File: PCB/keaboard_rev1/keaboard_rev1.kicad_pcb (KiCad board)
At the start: 2 copper layers, 6 parts, among them U1 Arduino Pro Micro

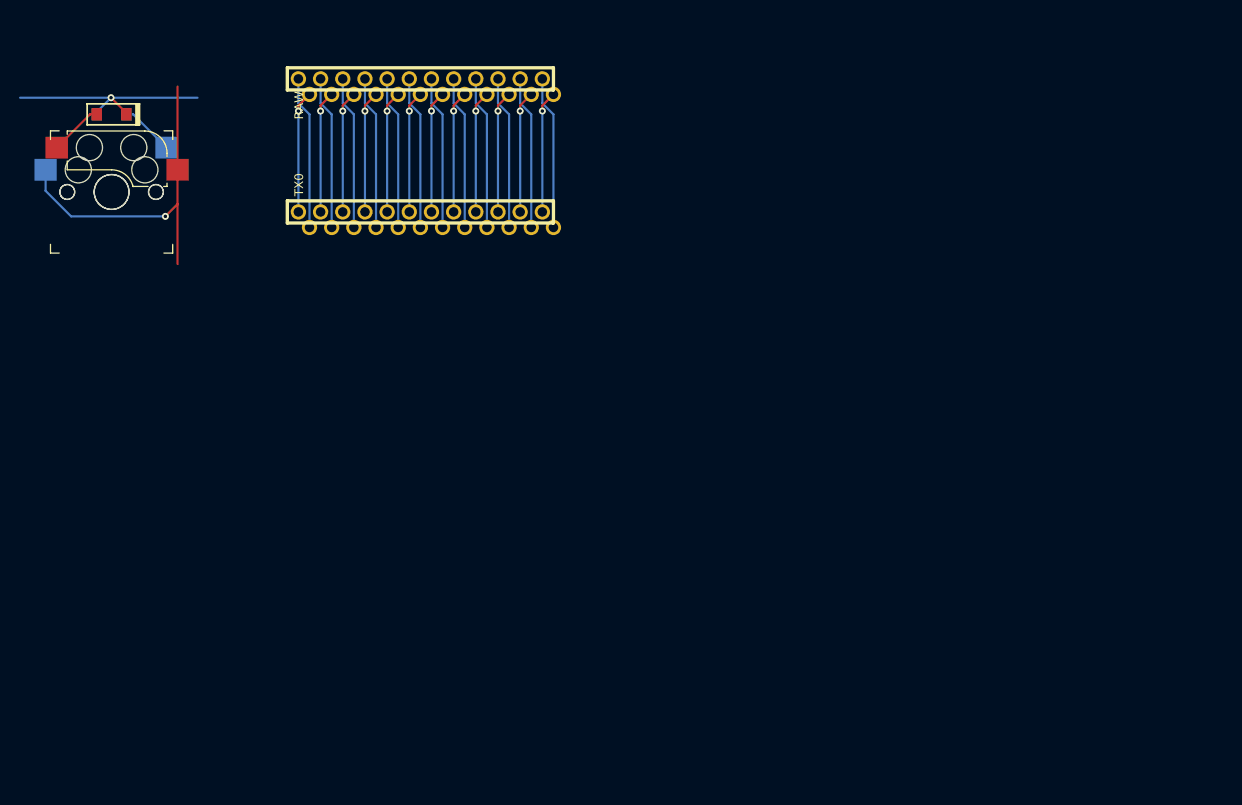
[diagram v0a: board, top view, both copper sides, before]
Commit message: Keyboard layout and cutout
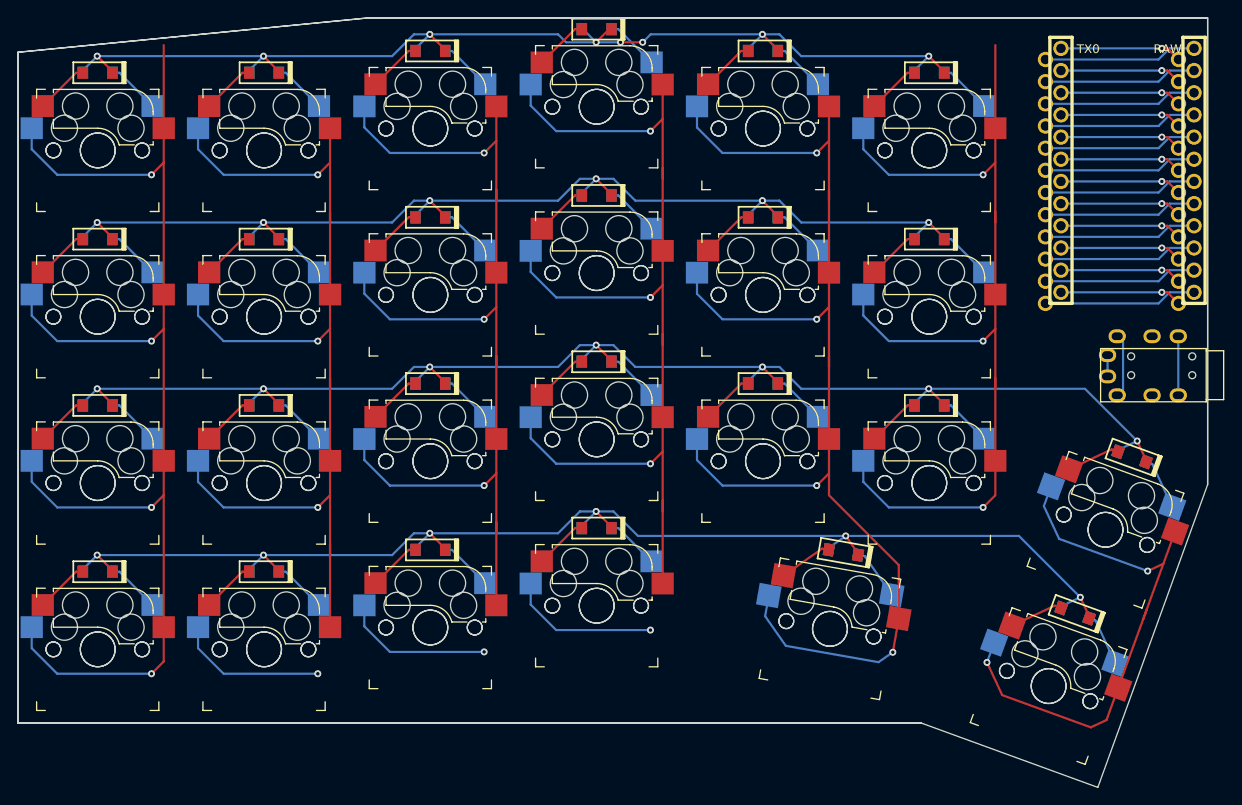
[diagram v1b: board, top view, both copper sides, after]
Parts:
- removed the D_SOD123 at (39.7, 38.7) (x2)
- removed the REF** at (39.7, 47.6) (x2)
- added D_SOD123: VAL**, keyboard_parts:D_SOD123, B.Cu at (150.1, 95.9)
- added D_SOD123: VAL**, keyboard_parts:D_SOD123, F.Cu at (133.3, 53.0)
- added D_SOD123: VAL**, keyboard_parts:D_SOD123, F.Cu at (114.3, 50.5)
- added D_SOD123: VAL**, keyboard_parts:D_SOD123, F.Cu at (95.2, 48.0)
- added D_SOD123: VAL**, keyboard_parts:D_SOD123, F.Cu at (133.3, 34.0)
- added D_SOD123: VAL**, keyboard_parts:D_SOD123, F.Cu at (114.3, 31.5)
- added D_SOD123: VAL**, keyboard_parts:D_SOD123, B.Cu at (123.5, 88.9)
- added D_SOD123: VAL**, keyboard_parts:D_SOD123, B.Cu at (95.2, 86.1)
- added D_SOD123: VAL**, keyboard_parts:D_SOD123, B.Cu at (133.3, 72.1)
- added D_SOD123: VAL**, keyboard_parts:D_SOD123, B.Cu at (114.3, 69.6)
- added D_SOD123: VAL**, keyboard_parts:D_SOD123, B.Cu at (95.2, 67.1)
- added D_SOD123: VAL**, keyboard_parts:D_SOD123, F.Cu at (150.1, 95.9)
- added D_SOD123: VAL**, keyboard_parts:D_SOD123, B.Cu at (133.3, 53.0)
- added D_SOD123: VAL**, keyboard_parts:D_SOD123, B.Cu at (114.3, 50.5)
- added D_SOD123: VAL**, keyboard_parts:D_SOD123, B.Cu at (95.2, 48.0)
- added D_SOD123: VAL**, keyboard_parts:D_SOD123, B.Cu at (133.3, 34.0)
- added D_SOD123: VAL**, keyboard_parts:D_SOD123, B.Cu at (114.3, 31.5)
- added D_SOD123: VAL**, keyboard_parts:D_SOD123, B.Cu at (76.2, 88.6)
- added D_SOD123: VAL**, keyboard_parts:D_SOD123, B.Cu at (57.1, 91.1)
- added D_SOD123: VAL**, keyboard_parts:D_SOD123, B.Cu at (76.2, 69.6)
- added D_SOD123: VAL**, keyboard_parts:D_SOD123, B.Cu at (57.1, 72.1)
- added D_SOD123: VAL**, keyboard_parts:D_SOD123, B.Cu at (76.2, 50.5)
- added D_SOD123: VAL**, keyboard_parts:D_SOD123, F.Cu at (156.6, 78.0)
- added D_SOD123: VAL**, keyboard_parts:D_SOD123, B.Cu at (57.1, 53.0)
- added D_SOD123: VAL**, keyboard_parts:D_SOD123, B.Cu at (95.2, 29.0)
- added D_SOD123: VAL**, keyboard_parts:D_SOD123, B.Cu at (76.2, 31.5)
- added D_SOD123: VAL**, keyboard_parts:D_SOD123, F.Cu at (76.2, 88.6)
- added D_SOD123: VAL**, keyboard_parts:D_SOD123, F.Cu at (57.1, 91.1)
- added D_SOD123: VAL**, keyboard_parts:D_SOD123, F.Cu at (76.2, 69.6)
- added D_SOD123: VAL**, keyboard_parts:D_SOD123, F.Cu at (57.1, 72.1)
- added D_SOD123: VAL**, keyboard_parts:D_SOD123, F.Cu at (76.2, 50.5)
- added D_SOD123: VAL**, keyboard_parts:D_SOD123, F.Cu at (57.1, 53.0)
- added D_SOD123: VAL**, keyboard_parts:D_SOD123, F.Cu at (95.2, 29.0)
- added D_SOD123: VAL**, keyboard_parts:D_SOD123, B.Cu at (156.6, 78.0)
- added D_SOD123: VAL**, keyboard_parts:D_SOD123, F.Cu at (76.2, 31.5)
- added D_SOD123: VAL**, keyboard_parts:D_SOD123, F.Cu at (38.1, 91.1)
- added D_SOD123: VAL**, keyboard_parts:D_SOD123, F.Cu at (38.1, 72.1)
- added D_SOD123: VAL**, keyboard_parts:D_SOD123, F.Cu at (38.1, 53.0)
- added D_SOD123: VAL**, keyboard_parts:D_SOD123, F.Cu at (57.1, 34.0)
- added D_SOD123: VAL**, keyboard_parts:D_SOD123, B.Cu at (38.1, 91.1)
- added D_SOD123: VAL**, keyboard_parts:D_SOD123, B.Cu at (38.1, 72.1)
- added D_SOD123: VAL**, keyboard_parts:D_SOD123, B.Cu at (38.1, 53.0)
- added D_SOD123: VAL**, keyboard_parts:D_SOD123, B.Cu at (57.1, 34.0)
- added D_SOD123: VAL**, keyboard_parts:D_SOD123, F.Cu at (38.1, 34.0)
- added D_SOD123: VAL**, keyboard_parts:D_SOD123, F.Cu at (123.5, 88.9)
- added D_SOD123: VAL**, keyboard_parts:D_SOD123, B.Cu at (38.1, 34.0)
- added D_SOD123: VAL**, keyboard_parts:D_SOD123, F.Cu at (95.2, 86.1)
- added D_SOD123: VAL**, keyboard_parts:D_SOD123, F.Cu at (133.3, 72.1)
- added D_SOD123: VAL**, keyboard_parts:D_SOD123, F.Cu at (114.3, 69.6)
- added D_SOD123: VAL**, keyboard_parts:D_SOD123, F.Cu at (95.2, 67.1)
- added REF**: Kailh_socket_MX, keyswitches:Kailh_socket_MX, B.Cu at (133.3, 81.0)
- added REF**: Kailh_socket_MX, keyswitches:Kailh_socket_MX, B.Cu at (95.2, 95.0)
- added REF**: Kailh_socket_MX, keyswitches:Kailh_socket_MX, B.Cu at (114.3, 78.5)
- added REF**: Kailh_socket_MX, keyswitches:Kailh_socket_MX, B.Cu at (95.2, 76.0)
- added REF**: Kailh_socket_MX, keyswitches:Kailh_socket_MX, B.Cu at (133.3, 61.9)
- added REF**: Kailh_socket_MX, keyswitches:Kailh_socket_MX, B.Cu at (114.3, 59.4)
- added REF**: Kailh_socket_MX, keyswitches:Kailh_socket_MX, B.Cu at (95.2, 56.9)
- added REF**: Kailh_socket_MX, keyswitches:Kailh_socket_MX, B.Cu at (133.3, 42.9)
- added REF**: Kailh_socket_MX, keyswitches:Kailh_socket_MX, B.Cu at (114.3, 40.4)
- added REF**: Kailh_socket_MX, keyswitches:Kailh_socket_MX, F.Cu at (122.0, 97.7)
- added REF**: Kailh_socket_MX, keyswitches:Kailh_socket_MX, F.Cu at (95.2, 95.0)
- added REF**: Kailh_socket_MX, keyswitches:Kailh_socket_MX, B.Cu at (38.1, 100.0)
- added REF**: Kailh_socket_MX, keyswitches:Kailh_socket_MX, F.Cu at (114.3, 78.5)
- added REF**: Kailh_socket_MX, keyswitches:Kailh_socket_MX, F.Cu at (95.2, 76.0)
- added REF**: Kailh_socket_MX, keyswitches:Kailh_socket_MX, F.Cu at (133.3, 61.9)
- added REF**: Kailh_socket_MX, keyswitches:Kailh_socket_MX, F.Cu at (114.3, 59.4)
- added REF**: Kailh_socket_MX, keyswitches:Kailh_socket_MX, F.Cu at (95.2, 56.9)
- added REF**: Kailh_socket_MX, keyswitches:Kailh_socket_MX, F.Cu at (133.3, 42.9)
- added REF**: Kailh_socket_MX, keyswitches:Kailh_socket_MX, F.Cu at (114.3, 40.4)
- added REF**: Kailh_socket_MX, keyswitches:Kailh_socket_MX, B.Cu at (76.2, 97.5)
- added REF**: Kailh_socket_MX, keyswitches:Kailh_socket_MX, B.Cu at (57.1, 100.0)
- added REF**: Kailh_socket_MX, keyswitches:Kailh_socket_MX, B.Cu at (76.2, 78.5)
- added REF**: Kailh_socket_MX, keyswitches:Kailh_socket_MX, B.Cu at (38.1, 81.0)
- added REF**: Kailh_socket_MX, keyswitches:Kailh_socket_MX, B.Cu at (57.1, 81.0)
- added REF**: Kailh_socket_MX, keyswitches:Kailh_socket_MX, B.Cu at (76.2, 59.4)
- added REF**: Kailh_socket_MX, keyswitches:Kailh_socket_MX, B.Cu at (57.1, 61.9)
- added REF**: Kailh_socket_MX, keyswitches:Kailh_socket_MX, B.Cu at (95.2, 37.9)
- added REF**: Kailh_socket_MX, keyswitches:Kailh_socket_MX, B.Cu at (76.2, 40.4)
- added REF**: Kailh_socket_MX, keyswitches:Kailh_socket_MX, F.Cu at (76.2, 97.5)
- added REF**: Kailh_socket_MX, keyswitches:Kailh_socket_MX, F.Cu at (57.1, 100.0)
- added REF**: Kailh_socket_MX, keyswitches:Kailh_socket_MX, F.Cu at (76.2, 78.5)
- added REF**: Kailh_socket_MX, keyswitches:Kailh_socket_MX, F.Cu at (57.1, 81.0)
- added REF**: Kailh_socket_MX, keyswitches:Kailh_socket_MX, F.Cu at (76.2, 59.4)
- added REF**: Kailh_socket_MX, keyswitches:Kailh_socket_MX, F.Cu at (133.3, 81.0)
- added REF**: Kailh_socket_MX, keyswitches:Kailh_socket_MX, F.Cu at (57.1, 61.9)
- added REF**: Kailh_socket_MX, keyswitches:Kailh_socket_MX, F.Cu at (95.2, 37.9)
- added REF**: Kailh_socket_MX, keyswitches:Kailh_socket_MX, F.Cu at (76.2, 40.4)
- added REF**: Kailh_socket_MX, keyswitches:Kailh_socket_MX, B.Cu at (38.1, 61.9)
- added REF**: Kailh_socket_MX, keyswitches:Kailh_socket_MX, B.Cu at (57.1, 42.9)
- added REF**: Kailh_socket_MX, keyswitches:Kailh_socket_MX, F.Cu at (38.1, 100.0)
- added REF**: Kailh_socket_MX, keyswitches:Kailh_socket_MX, F.Cu at (38.1, 81.0)
- added REF**: Kailh_socket_MX, keyswitches:Kailh_socket_MX, F.Cu at (38.1, 61.9)
- added REF**: Kailh_socket_MX, keyswitches:Kailh_socket_MX, F.Cu at (57.1, 42.9)
- added REF**: Kailh_socket_MX, keyswitches:Kailh_socket_MX, F.Cu at (38.1, 42.9)
- added REF**: Kailh_socket_MX, keyswitches:Kailh_socket_MX, F.Cu at (147.0, 104.2)
- added REF**: Kailh_socket_MX, keyswitches:Kailh_socket_MX, B.Cu at (38.1, 42.9)
- added REF**: TRRS-PJ-320A, Keebio-Parts:TRRS-PJ-320A, B.Cu at (165.1, 66.5)
- added REF**: TRRS-PJ-320A, Keebio-Parts:TRRS-PJ-320A, F.Cu at (165.1, 68.6)
- added REF**: Kailh_socket_MX, keyswitches:Kailh_socket_MX, B.Cu at (147.0, 104.2)
- added REF**: Kailh_socket_MX, keyswitches:Kailh_socket_MX, B.Cu at (153.5, 86.3)
- added REF**: Kailh_socket_MX, keyswitches:Kailh_socket_MX, F.Cu at (153.5, 86.3)
- added REF**: Kailh_socket_MX, keyswitches:Kailh_socket_MX, B.Cu at (122.0, 97.7)
- moved U1 81.0 mm to (156.1, 45.1), turned to 270 degrees
- moved U1 78.0 mm to (154.3, 46.4), turned to 270 degrees
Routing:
- net (no net): track 455.9 -> 2152.8 mm, vias 14 -> 64
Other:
- board outline added: 136.3 x 88.1 mm

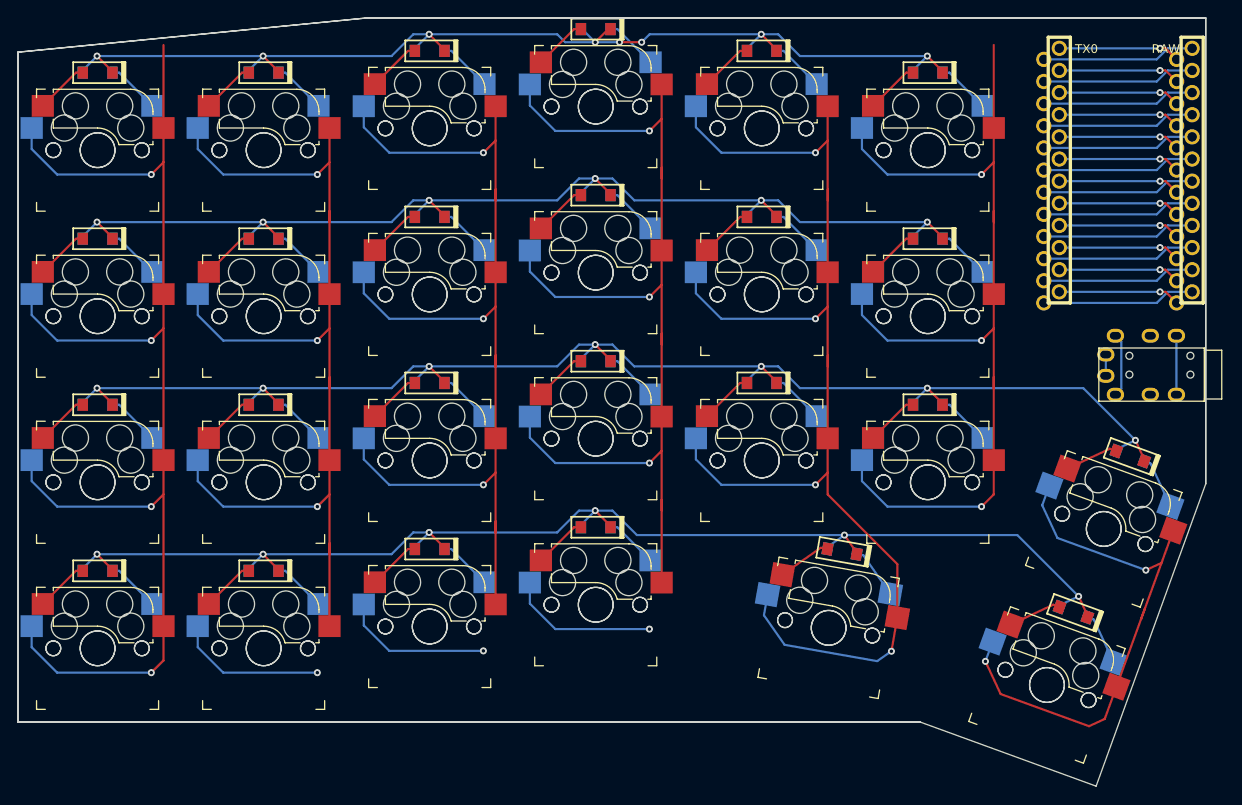
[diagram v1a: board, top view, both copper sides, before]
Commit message: Add reset switch, add power switch, add docs
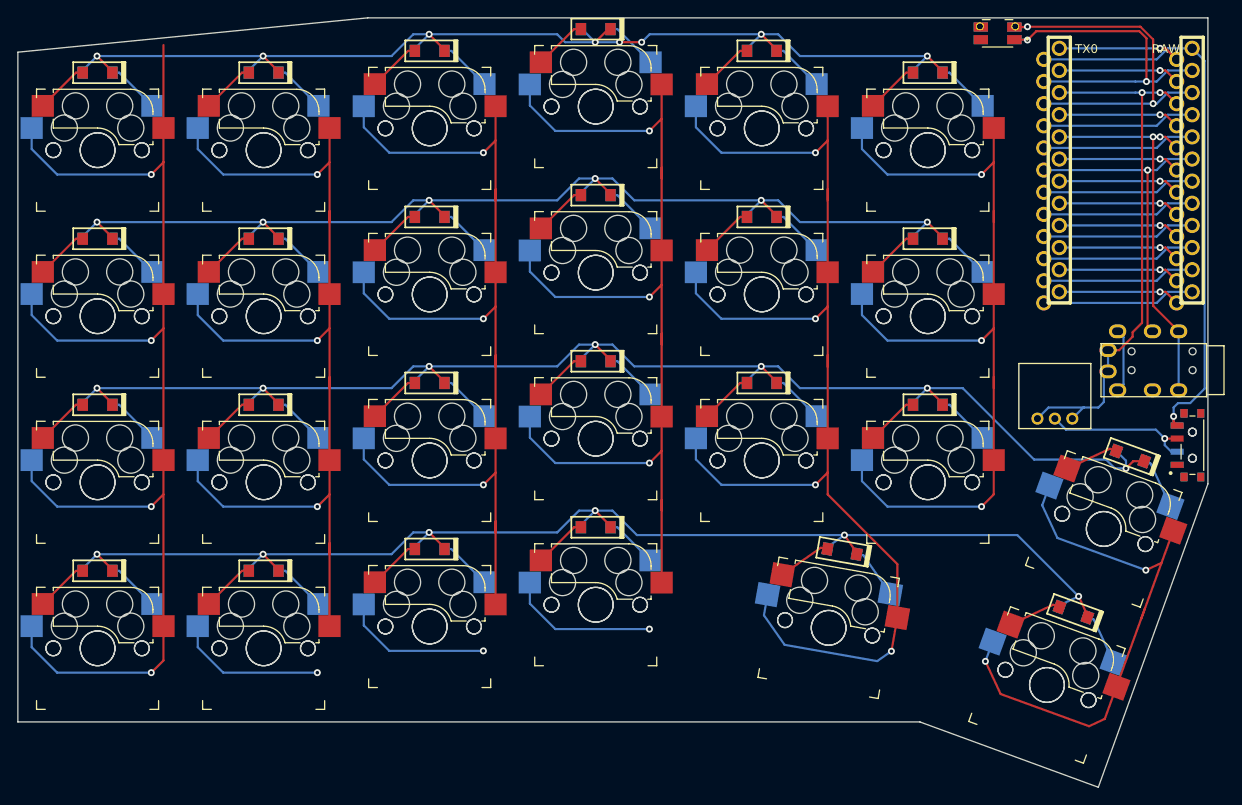
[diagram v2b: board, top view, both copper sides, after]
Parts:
- added REF**: SW_EVQ-9P701P, parts:SW_EVQ-9P701P, B.Cu at (141.4, 29.5)
- added REF**: SW_EVQ-9P701P, parts:SW_EVQ-9P701P, F.Cu at (141.4, 29.5)
- added REF**: SW_PCM12SMTR, parts:SW_PCM12SMTR, B.Cu at (163.7, 76.7)
- added REF**: SW_PCM12SMTR, parts:SW_PCM12SMTR, F.Cu at (163.7, 76.7)
- added REF**: CON3_1X3_R_DF3, parts:DF3A-3P-2DS, F.Cu at (145.9, 73.7)
- moved REF** 0.57 mm to (165.3, 65.9)
- moved REF** 0.57 mm to (165.3, 68.1)
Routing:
- net (no net): track 2152.8 -> 2344.2 mm, vias 64 -> 73
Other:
- board size 136.3 x 88.1 mm -> 136.5 x 88.3 mm

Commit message: Route traces for matrix
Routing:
- net (no net): track 2344.2 -> 2899.5 mm, vias 73 -> 87

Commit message: Add label, update README
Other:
- board text added: "designed by keawade"
- board text added: "keaboard"
- board text added: "rev1"
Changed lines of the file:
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@@
   (general
     (thickness 1.6)
-    (drawings 7)
+    (drawings 13)
     (tracks 718)
     (zones 0)
@@
     )
   )
+  (gr_text "designed by keawade" (at 156.972 47.244 90) (layer B.SilkS)
+    (effects (font (size 1.5 1.5) (thickness 0.3)) (justify mirror))
+  )
+  (gr_text rev1 (at 154.432 56.769 90) (layer B.SilkS)
+    (effects (font (size 1.5 1.5) (thickness 0.3)) (justify mirror))
+  )
+  (gr_text keaboard (at 153.67 43.561 90) (layer B.SilkS)
+    (effects (font (size 3 3) (thickness 0.5)) (justify mirror))
+  )
+  (gr_text "designed by keawade" (at 156.972 45.72 90) (layer F.SilkS)
+    (effects (font (size 1.5 1.5) (thickness 0.3)))
+  )
+  (gr_text keaboard (at 153.67 49.276 90) (layer F.SilkS)
+    (effects (font (size 3 3) (thickness 0.5)))
+  )
+  (gr_text rev1 (at 154.432 36.068 90) (layer F.SilkS)
+    (effects (font (size 1.5 1.5) (thickness 0.3)))
+  )
   (gr_line (start 165.481 27.686) (end 165.481 81.153) (layer Edge.Cuts) (width 0.1))

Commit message: WIP, created WIP reversible footprints, created schematic, updated board with schematic
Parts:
- removed D_SOD123 (x50): VAL**, keyboard_parts:D_SOD123
- removed REF** (x2): SW_EVQ-9P701P, parts:SW_EVQ-9P701P
- removed REF** (x50): Kailh_socket_MX, keyswitches:Kailh_socket_MX
- removed REF** (x2): SW_PCM12SMTR, parts:SW_PCM12SMTR
- removed REF**: CON3_1X3_R_DF3, parts:DF3A-3P-2DS
- removed REF** (x2): TRRS-PJ-320A, Keebio-Parts:TRRS-PJ-320A
- removed the U1 at (154.3, 46.4)
- removed the U1 at (156.1, 45.1)
- added D01: D, parts:D_SOD123_reversible, F.Cu at (146.2, 107.9)
- added D01: D, parts:D_SOD123_reversible, F.Cu at (95.6, 98.8)
- added D01: D, parts:D_SOD123_reversible, F.Cu at (95.6, 79.7)
- added D01: D, parts:D_SOD123_reversible, F.Cu at (95.6, 60.7)
- added D01: D, parts:D_SOD123_reversible, F.Cu at (95.6, 41.6)
- added D01: D, parts:D_SOD123_reversible, F.Cu at (76.6, 101.3)
- added D01: D, parts:D_SOD123_reversible, F.Cu at (76.6, 82.2)
- added D01: D, parts:D_SOD123_reversible, F.Cu at (76.6, 63.2)
- added D01: D, parts:D_SOD123_reversible, F.Cu at (76.6, 44.1)
- added D01: D, parts:D_SOD123_reversible, F.Cu at (57.5, 103.8)
- added D01: D, parts:D_SOD123_reversible, F.Cu at (57.5, 84.7)
- added D01: D, parts:D_SOD123_reversible, F.Cu at (152.7, 90.0)
- added D01: D, parts:D_SOD123_reversible, F.Cu at (57.5, 65.7)
- added D01: D, parts:D_SOD123_reversible, F.Cu at (57.5, 46.6)
- added D01: D, parts:D_SOD123_reversible, F.Cu at (38.5, 103.8)
- added D01: D, parts:D_SOD123_reversible, F.Cu at (38.5, 65.7)
- added D01: D, parts:D_SOD123_reversible, F.Cu at (38.5, 46.6)
- added D01: D, parts:D_SOD123_reversible, F.Cu at (122.1, 101.6)
- added D01: D, parts:D_SOD123_reversible, F.Cu at (133.7, 84.7)
- added D01: D, parts:D_SOD123_reversible, F.Cu at (133.7, 65.7)
- added D01: D, parts:D_SOD123_reversible, F.Cu at (133.7, 46.6)
- added D01: D, parts:D_SOD123_reversible, F.Cu at (114.7, 82.2)
- added D01: D, parts:D_SOD123_reversible, F.Cu at (114.7, 63.2)
- added D01: D, parts:D_SOD123_reversible, F.Cu at (114.7, 44.1)
- added D02: D, parts:D_SOD123_reversible, F.Cu at (76.2, 2.92)
- added D03: D, parts:D_SOD123_reversible, F.Cu at (38.4, 84.7)
- added D04: D, parts:D_SOD123_reversible, F.Cu at (197.3, -58.1)
- added D05: D, parts:D_SOD123_reversible, F.Cu at (189.7, -50.9)
- added D06: D, parts:D_SOD123_reversible, F.Cu at (189.7, -54.5)
- added D07: D, parts:D_SOD123_reversible, F.Cu at (129.4, 6.52)
- added D08: D, parts:D_SOD123_reversible, F.Cu at (121.8, 6.52)
- added D09: D, parts:D_SOD123_reversible, F.Cu at (189.7, -58.1)
- added D10: D, parts:D_SOD123_reversible, F.Cu at (197.3, -61.7)
- added D11: D, parts:D_SOD123_reversible, F.Cu at (129.4, 2.92)
- added D12: D, parts:D_SOD123_reversible, F.Cu at (189.7, -61.7)
- added D13: D, parts:D_SOD123_reversible, F.Cu at (121.8, 2.92)
- added D14: D, parts:D_SOD123_reversible, F.Cu at (189.7, -47.3)
- added D15: D, parts:D_SOD123_reversible, F.Cu at (76.2, 6.52)
- added D16: D, parts:D_SOD123_reversible, F.Cu at (83.8, 2.92)
- added D17: D, parts:D_SOD123_reversible, F.Cu at (91.4, 2.92)
- added D18: D, parts:D_SOD123_reversible, F.Cu at (83.8, 6.52)
- added D19: D, parts:D_SOD123_reversible, F.Cu at (91.4, 6.52)
- added D20: D, parts:D_SOD123_reversible, F.Cu at (99.0, 2.92)
- added D21: D, parts:D_SOD123_reversible, F.Cu at (99.0, 6.52)
- added D22: D, parts:D_SOD123_reversible, F.Cu at (106.6, 2.92)
- added D23: D, parts:D_SOD123_reversible, F.Cu at (106.6, 6.52)
- added D24: D, parts:D_SOD123_reversible, F.Cu at (114.2, 2.92)
- added D25: D, parts:D_SOD123_reversible, F.Cu at (114.2, 6.52)
- added K01: KEYSW, parts:Kailh_socket_MX_reversible, B.Cu at (147.5, 104.0)
- added K01: KEYSW, parts:Kailh_socket_MX_reversible, B.Cu at (95.5, 94.6)
- added K01: KEYSW, parts:Kailh_socket_MX_reversible, B.Cu at (95.5, 75.5)
- added K01: KEYSW, parts:Kailh_socket_MX_reversible, B.Cu at (95.5, 56.5)
- added K01: KEYSW, parts:Kailh_socket_MX_reversible, B.Cu at (95.5, 37.4)
- added K01: KEYSW, parts:Kailh_socket_MX_reversible, B.Cu at (76.5, 97.1)
- added K01: KEYSW, parts:Kailh_socket_MX_reversible, B.Cu at (76.5, 78.0)
- added K01: KEYSW, parts:Kailh_socket_MX_reversible, B.Cu at (76.5, 59.0)
- added K01: KEYSW, parts:Kailh_socket_MX_reversible, B.Cu at (76.5, 39.9)
- added K01: KEYSW, parts:Kailh_socket_MX_reversible, B.Cu at (57.4, 99.6)
- added K01: KEYSW, parts:Kailh_socket_MX_reversible, B.Cu at (57.4, 80.5)
- added K01: KEYSW, parts:Kailh_socket_MX_reversible, B.Cu at (154.0, 86.1)
- added K01: KEYSW, parts:Kailh_socket_MX_reversible, B.Cu at (57.4, 61.5)
- added K01: KEYSW, parts:Kailh_socket_MX_reversible, B.Cu at (57.4, 42.4)
- added K01: KEYSW, parts:Kailh_socket_MX_reversible, B.Cu at (38.4, 99.6)
- added K01: KEYSW, parts:Kailh_socket_MX_reversible, B.Cu at (38.4, 61.5)
- added K01: KEYSW, parts:Kailh_socket_MX_reversible, B.Cu at (38.4, 42.4)
- added K01: KEYSW, parts:Kailh_socket_MX_reversible, B.Cu at (122.7, 97.4)
- added K01: KEYSW, parts:Kailh_socket_MX_reversible, B.Cu at (133.6, 80.5)
- added K01: KEYSW, parts:Kailh_socket_MX_reversible, B.Cu at (133.6, 61.5)
- added K01: KEYSW, parts:Kailh_socket_MX_reversible, B.Cu at (133.6, 42.4)
- added K01: KEYSW, parts:Kailh_socket_MX_reversible, B.Cu at (114.6, 78.0)
- added K01: KEYSW, parts:Kailh_socket_MX_reversible, B.Cu at (114.6, 59.0)
- added K01: KEYSW, parts:Kailh_socket_MX_reversible, B.Cu at (114.6, 39.9)
- added K02: KEYSW, parts:Kailh_socket_MX_reversible, B.Cu at (136.4, -7.08)
- added K03: KEYSW, parts:Kailh_socket_MX_reversible, B.Cu at (38.4, 80.5)
- added K04: KEYSW, parts:Kailh_socket_MX_reversible, B.Cu at (117.5, -23.2)
- added K05: KEYSW, parts:Kailh_socket_MX_reversible, B.Cu at (98.5, -39.4)
- added K06: KEYSW, parts:Kailh_socket_MX_reversible, B.Cu at (79.6, -55.5)
- added K07: KEYSW, parts:Kailh_socket_MX_reversible, B.Cu at (117.5, -7.08)
- added K08: KEYSW, parts:Kailh_socket_MX_reversible, B.Cu at (98.5, -23.2)
- added K09: KEYSW, parts:Kailh_socket_MX_reversible, B.Cu at (79.6, -39.4)
- added K10: KEYSW, parts:Kailh_socket_MX_reversible, B.Cu at (98.5, -7.08)
- added K11: KEYSW, parts:Kailh_socket_MX_reversible, B.Cu at (79.6, -23.2)
- added K12: KEYSW, parts:Kailh_socket_MX_reversible, B.Cu at (79.6, -7.08)
- added K13: KEYSW, parts:Kailh_socket_MX_reversible, B.Cu at (98.5, -55.5)
- added K14: KEYSW, parts:Kailh_socket_MX_reversible, B.Cu at (174.2, -39.4)
- added K15: KEYSW, parts:Kailh_socket_MX_reversible, B.Cu at (117.5, -39.4)
- added K16: KEYSW, parts:Kailh_socket_MX_reversible, B.Cu at (136.4, -23.2)
- added K17: KEYSW, parts:Kailh_socket_MX_reversible, B.Cu at (155.3, -7.08)
- added K18: KEYSW, parts:Kailh_socket_MX_reversible, B.Cu at (117.5, -55.5)
- added K19: KEYSW, parts:Kailh_socket_MX_reversible, B.Cu at (136.4, -39.4)
- added K20: KEYSW, parts:Kailh_socket_MX_reversible, B.Cu at (155.3, -23.2)
- added K21: KEYSW, parts:Kailh_socket_MX_reversible, B.Cu at (174.2, -7.08)
- added K22: KEYSW, parts:Kailh_socket_MX_reversible, B.Cu at (136.4, -55.5)
- added K23: KEYSW, parts:Kailh_socket_MX_reversible, B.Cu at (155.3, -39.4)
- added K24: KEYSW, parts:Kailh_socket_MX_reversible, B.Cu at (174.2, -23.2)
- added K25: KEYSW, parts:Kailh_socket_MX_reversible, B.Cu at (155.3, -55.5)
- added SW_PWR1: SW_Push_SPDT, parts:SW_PCM12SMTR_reversible, F.Cu at (163.8, 76.5)
- added SW_RST1: SW_EVQ-9P701P, parts:SW_EVQ-9P701P_reversible, F.Cu at (141.4, 29.5)
- added TRRS1: TRRS Jack, parts:TRRS-PJ-320A_reversible, F.Cu at (165.5, 68.3)
- added U1: ProMicro, parts:ArduinoProMicro_Reversible, F.Cu at (155.8, 44.6)
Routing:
- net (no net): track 2899.5 -> 0.00 mm, vias 87 -> 0
- net TRRS_TIP: track 0.00 -> 47.7 mm, vias 0 -> 1
- net TRRS_SLEEVE: track 0.00 -> 43.5 mm, vias 0 -> 2
- net PWR: track 0.00 -> 17.3 mm
- net RST: track 0.00 -> 17.3 mm
- net Net-(U1-Pad21): track 0.00 -> 17.3 mm
- net COL3: track 0.00 -> 17.3 mm
- net COL2: track 0.00 -> 17.3 mm
- net Net-(U1-Pad20): track 0.00 -> 17.3 mm
- net COL7: track 0.00 -> 17.3 mm
- net COL6: track 0.00 -> 17.3 mm
- net COL5: track 0.00 -> 17.3 mm
- net COL4: track 0.00 -> 17.3 mm
- net ROW4: track 0.00 -> 14.3 mm, vias 0 -> 1
- net COL1: track 0.00 -> 14.3 mm, vias 0 -> 1
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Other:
- board size 136.5 x 88.3 mm -> 136.5 x 87.7 mm
- net class Default: trace_width 0.25 -> 0.254
- net class Power added: clearance 0.2, trace_width 0.381, via_dia 0.8, via_drill 0.4
